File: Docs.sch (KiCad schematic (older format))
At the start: 0 parts

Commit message: Sent to JLCPCB
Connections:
- wire segments 150 -> 417
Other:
- note added: "CKE"
- note added: "CMD (read)"
- note added: "CMD (write)"
- note added: "Information may be out of date. See ./cpld/RAM2E.v"
- note added: "MD[7:0] (read)"
- note added: "MD[7:0] (write)"
- note added: "S1"
- note added: "S2"
- note added: "S3"
- note added: "S4"
- note added: "S5"
- note added: "S6"
- note added: "S7"
- note added: "S8"
- note added: "S9"
- note added: "SA"
- note added: "SB"
- note added: "SC"
- note added: "SD"
- note added: "SE"
- note added: "State"
- note added: "VD[7:0]"
- note added: "old read data"
- note added: "read data"
- note added: "write data"
- note removed: "(latency)"
- note removed: "(reg. MD)"
- note removed: "(reg. VD)"
- note removed: "(reg. addr.)"
- note removed: "Information may be out of date,\nsuperseded by ./cpld/RAM2E.v"
- note removed: "State = { PHI0, C7M, nPRAS, nPCAS, Q3 }"

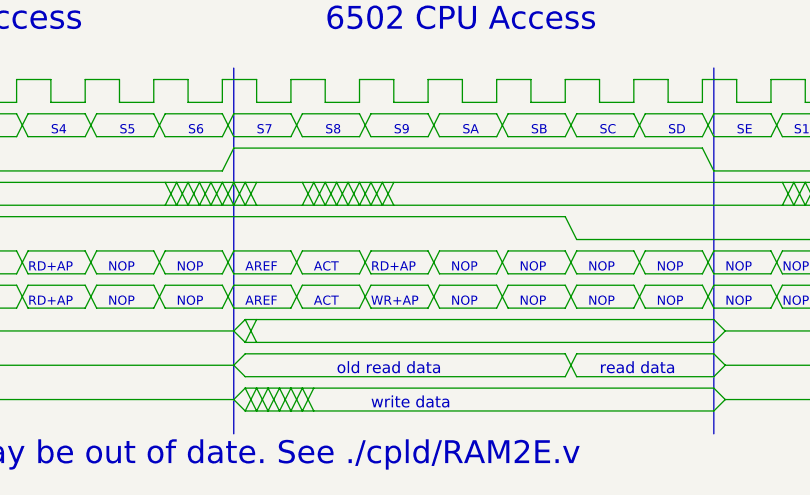
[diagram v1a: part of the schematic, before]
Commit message: Added jumper, new state machine docs
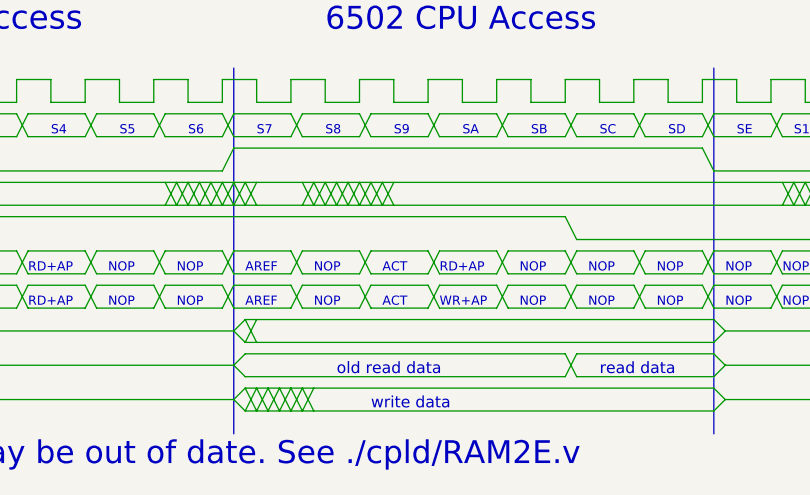
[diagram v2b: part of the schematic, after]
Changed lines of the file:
@@
 encoding utf-8
 Sheet 2 2
-Title "RAM2E"
-Date "2019-10-13"
+Title "RAM2E II"
+Date "2020-05-06"
 Rev "0.9"
 Comp "Garrett's Workshop"
@@
 Wire Wire Line
 	8600 2400 8750 2400
-Text Notes 6800 2250 0    40   ~ 0
+Text Notes 7100 2250 0    40   ~ 0
 RD+AP
-Text Notes 6550 2250 0    40   ~ 0
+Text Notes 6850 2250 0    40   ~ 0
 ACT
-Text Notes 7150 2250 0    40   ~ 0
-NOP
 Text Notes 7450 2250 0    40   ~ 0
 NOP
@@
 Text Notes 5300 2400 0    40   ~ 0
 RD+AP
-Text Notes 6550 2400 0    40   ~ 0
-ACT
-Text Notes 6800 2400 0    40   ~ 0
+Text Notes 7100 2400 0    40   ~ 0
 WR+AP
-Text Notes 7150 2400 0    40   ~ 0
-NOP
 Text Notes 7450 2400 0    40   ~ 0
 NOP
@@
 Text Notes 4150 3100 0    100  ~ 0
 Information may be out of date. See ./cpld/RAM2E.v
+Text Notes 6850 2400 0    40   ~ 0
+ACT
+Text Notes 6550 2250 0    40   ~ 0
+NOP
+Text Notes 6550 2400 0    40   ~ 0
+NOP
 $EndSCHEMATC
